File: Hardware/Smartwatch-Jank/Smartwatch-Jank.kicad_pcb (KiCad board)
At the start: 4 copper layers, 13 parts, among them U1 2472

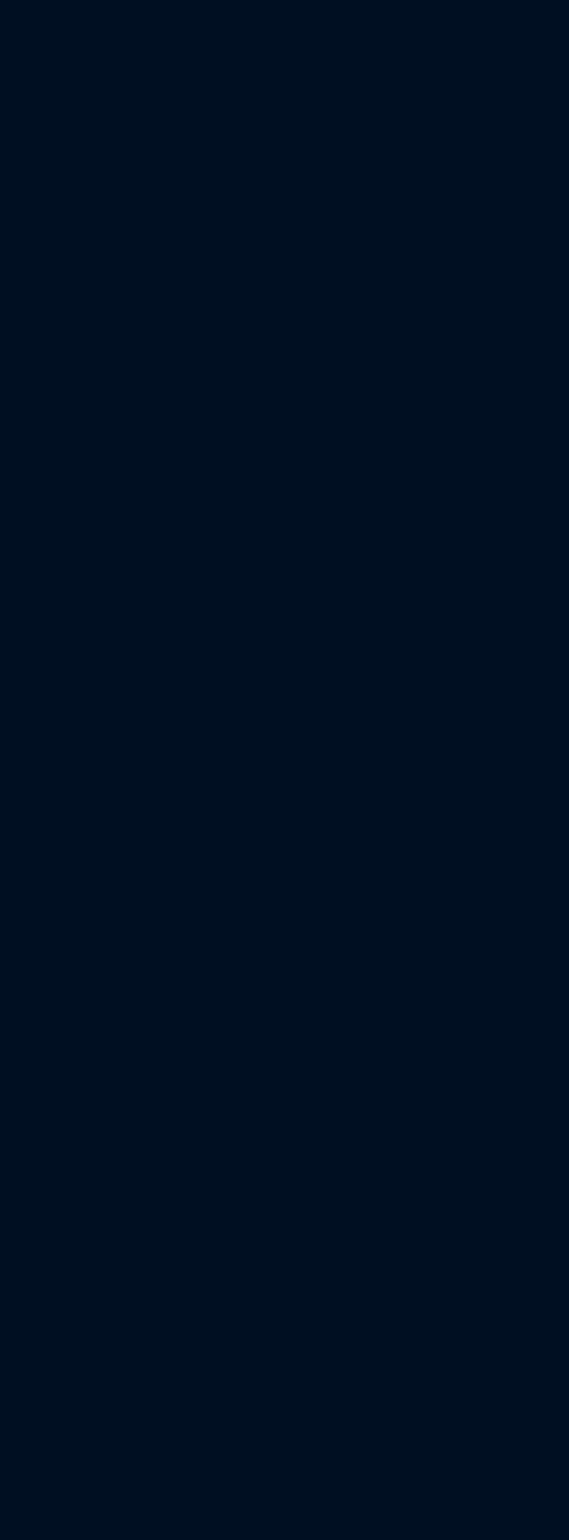
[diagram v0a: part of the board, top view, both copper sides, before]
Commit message: Replaced BNO055 to ICM20248 for more accurate IMU tracking
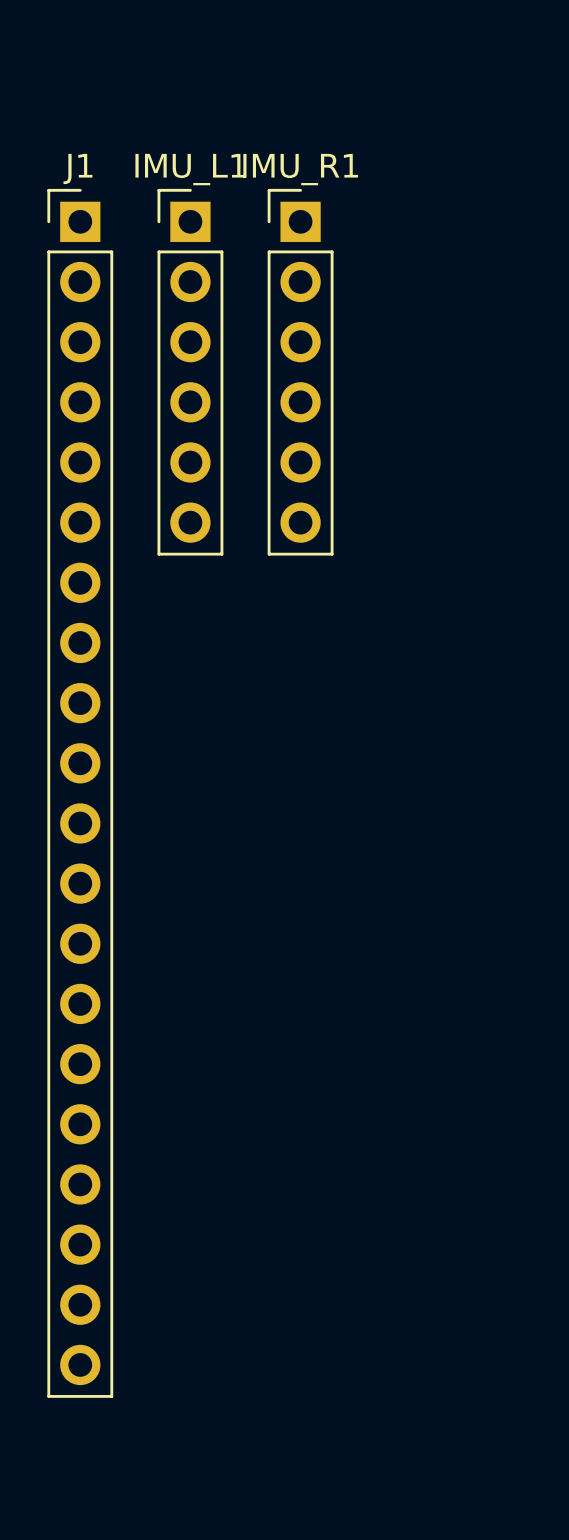
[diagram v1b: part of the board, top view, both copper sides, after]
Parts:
- added IMU_L1: Conn_01x06, Connector_PinHeader_2.54mm:PinHeader_1x06_P2.54mm_Vertical, F.Cu at (65.2, 43.2)
- added IMU_R1: Conn_01x06, Connector_PinHeader_2.54mm:PinHeader_1x06_P2.54mm_Vertical, F.Cu at (69.9, 43.2)
- added J1: Conn_01x20, Connector_PinHeader_2.54mm:PinHeader_1x20_P2.54mm_Vertical, F.Cu at (60.6, 43.2)
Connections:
- A1 pad 10: unconnected-(A1-D7-Pad10) -> /CCS
- A1 pad 11: unconnected-(A1-D8-Pad11) -> /D8
- A1 pad 12: unconnected-(A1-D9-Pad12) -> /D9
- A1 pad 13: /D10 -> unconnected-(A1-D10-Pad13)
- A1 pad 14: unconnected-(A1-MOSI-Pad14) -> /MOSI
- A1 pad 15: unconnected-(A1-MISO-Pad15) -> /MISO
- A1 pad 16: unconnected-(A1-SCK-Pad16) -> /SCK
- A1 pad 21: unconnected-(A1-A2-Pad21) -> /Y+
- A1 pad 22: unconnected-(A1-A3-Pad22) -> /X-
- A1 pad 29: GND -> /GND
- A1 pad 3: unconnected-(A1-~{RESET}-Pad3) -> /RST
- A1 pad 4: GND -> /GND
- A1 pad 5: unconnected-(A1-D2-Pad5) -> /CS
- A1 pad 6: unconnected-(A1-D3-Pad6) -> /D/C
- A1 pad 7: /D4 -> /X+
- A1 pad 8: /D5 -> /Y-
- A1 pad 9: unconnected-(A1-D6-Pad9) -> /Lite
- HR_Sensor1 pad 1: /D4 -> /D8
- HR_Sensor1 pad 5: GND -> /GND
- HR_Sensor_1 pad 1: /D5 -> /D9
- Pressure_Sensor1 pad 2: GND -> /GND
- USBC1 pad 2: GND -> /GND
- Vibration_Motor1 pad 2: GND -> /GND
- Voltage_Regulator1 pad 3: GND -> /GND
